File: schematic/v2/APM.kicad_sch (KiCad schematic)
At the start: 13 parts, among them J12 AUDIO_OUT, J4 LCD_display, U1 NUCLEO-H753ZI

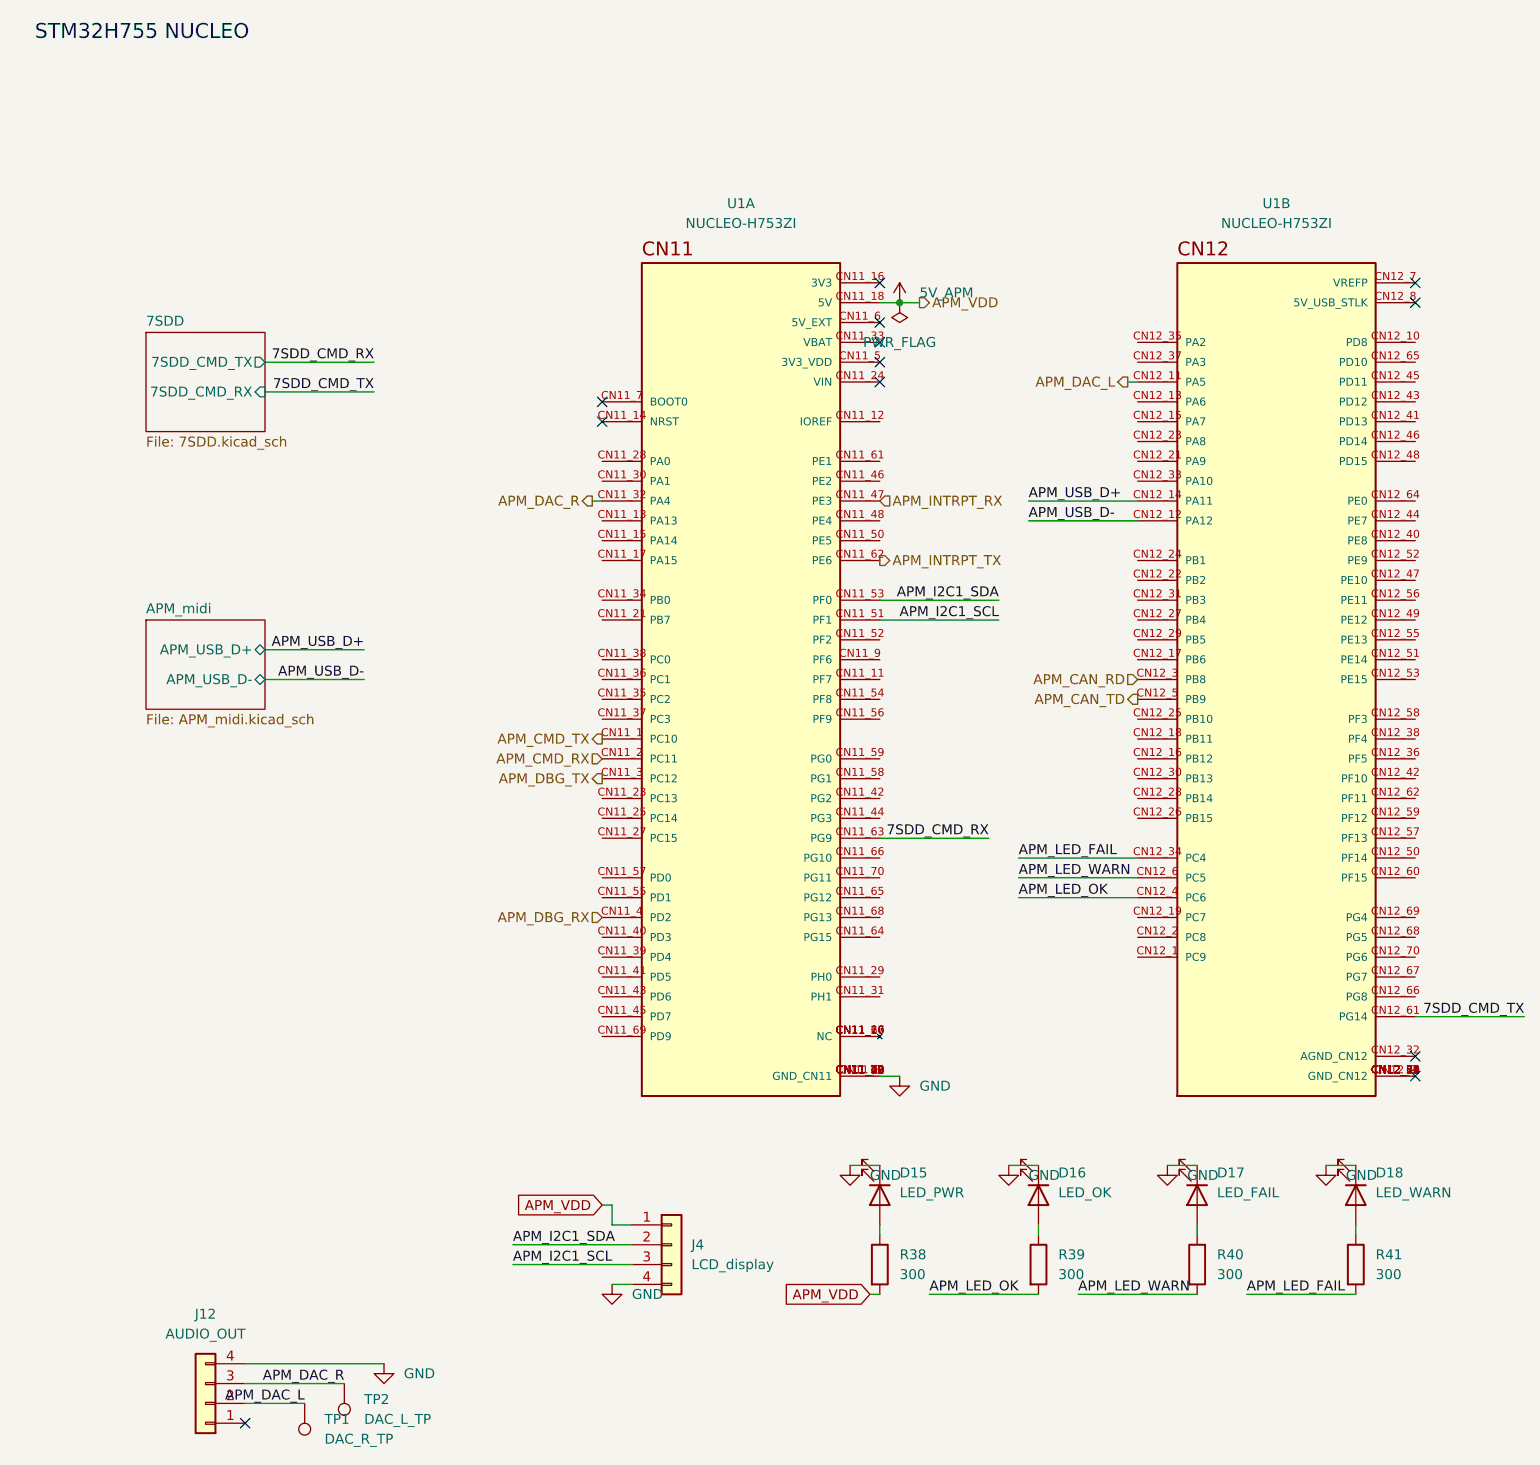
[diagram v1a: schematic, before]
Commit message: now making a v3 with HATs for each nucleo with my needed shit. this will make things very compact and hopefully much cheaper
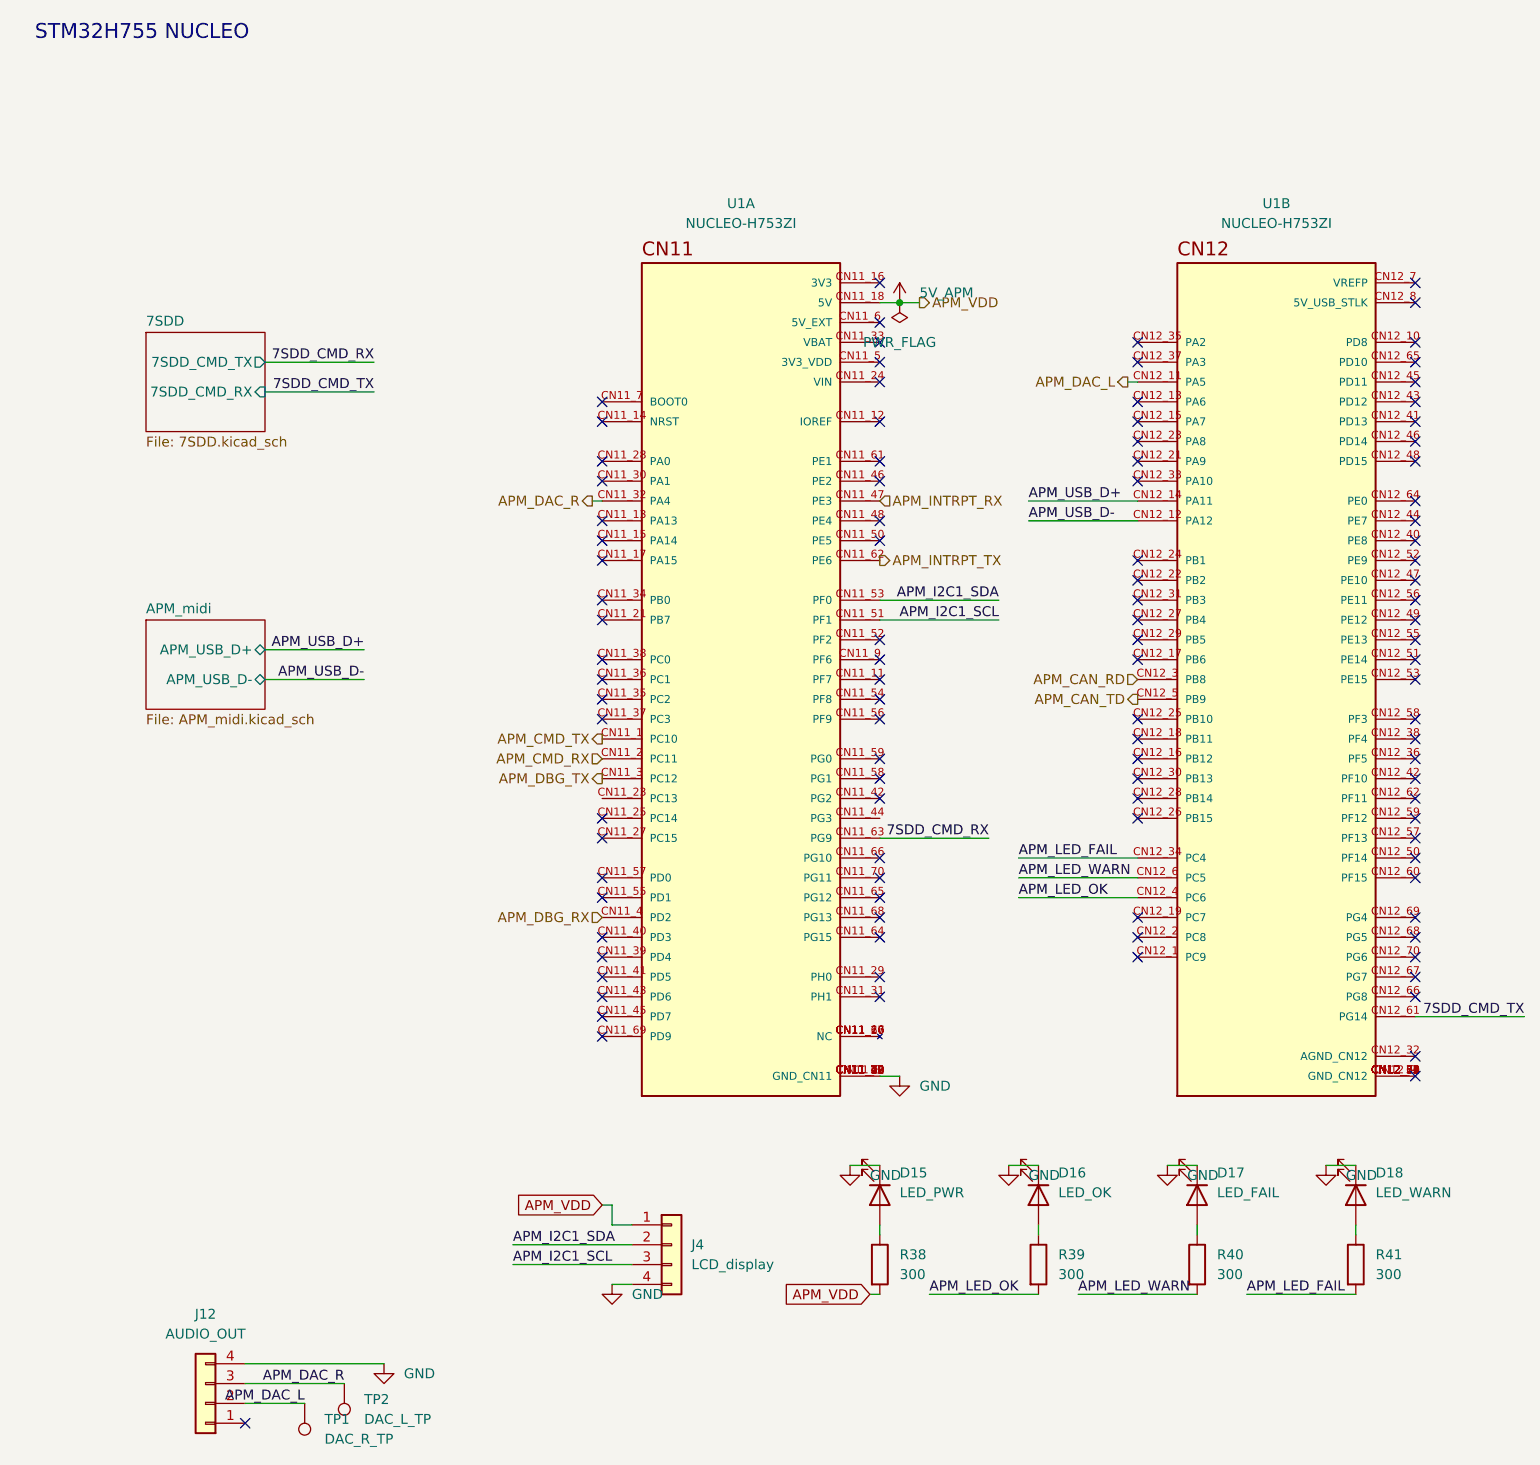
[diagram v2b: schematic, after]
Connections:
- no-connect marks 12 -> 106
